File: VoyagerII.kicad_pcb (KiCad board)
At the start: 2 copper layers, 285 x 95.1 mm, 265 parts, among them P1 TC2030-IDC, SW1 SW_PUSH, U1 ATXMEGA32A4U-AU, U2 MCP1700T-3002E/TT, U3 PRTR5V0U2X, U4 IS31FL3731-SALS2, U5 74LVC1G34

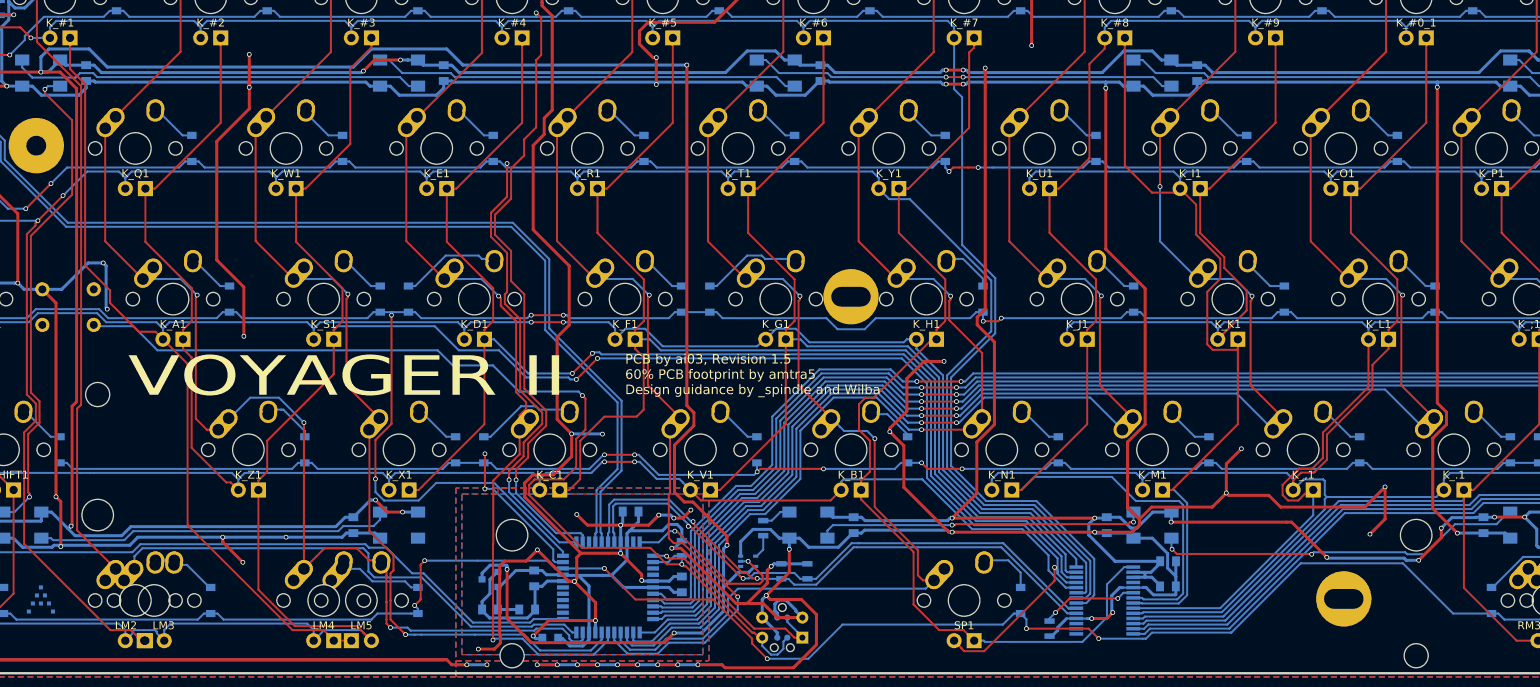
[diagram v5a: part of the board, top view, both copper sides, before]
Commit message: Tune up some traces
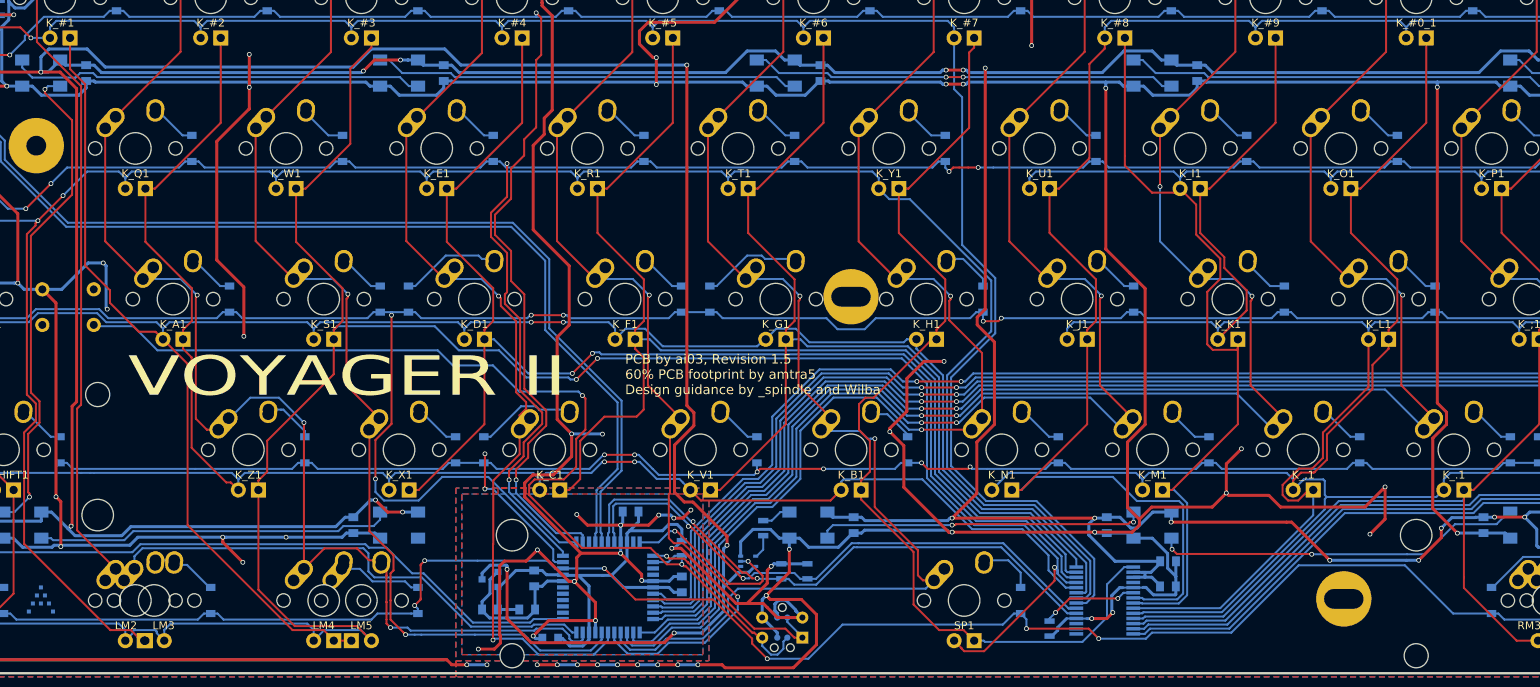
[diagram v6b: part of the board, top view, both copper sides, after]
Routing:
- net LED-B4: track 279.0 -> 278.2 mm
- net COL6: track 141.3 -> 142.0 mm
- net ROW2: track 334.0 -> 334.6 mm

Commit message: Unroute, prepare for LED chip replacement
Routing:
- net GND: track 1590.9 -> 0.00 mm, vias 74 -> 0
- net +5V: track 840.9 -> 0.00 mm, vias 22 -> 0
- net ROW0: track 340.1 -> 0.00 mm, vias 4 -> 0
- net LED-A1: track 336.7 -> 0.00 mm, vias 1 -> 0
- net ROW2: track 334.6 -> 0.00 mm, vias 6 -> 0
- net ROW1: track 327.0 -> 0.00 mm, vias 6 -> 0
- net COL14: track 316.5 -> 0.00 mm, vias 4 -> 0
- net LED-A5: track 301.0 -> 0.00 mm, vias 3 -> 0
- net LED-A2: track 294.3 -> 0.00 mm, vias 2 -> 0
- net LED-A3: track 279.0 -> 0.00 mm, vias 2 -> 0
- net LED-B4: track 278.2 -> 0.00 mm
- net ROW4: track 273.0 -> 0.00 mm, vias 6 -> 0
- net COL13: track 271.2 -> 0.00 mm, vias 4 -> 0
- net ROW3: track 267.4 -> 0.00 mm, vias 8 -> 0
- net COL12: track 258.2 -> 0.00 mm, vias 3 -> 0
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
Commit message: never mind
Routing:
- net GND: track 0.00 -> 1590.9 mm, vias 0 -> 74
- net +5V: track 0.00 -> 840.9 mm, vias 0 -> 22
- net ROW0: track 0.00 -> 340.1 mm, vias 0 -> 4
- net LED-A1: track 0.00 -> 336.7 mm, vias 0 -> 1
- net ROW2: track 0.00 -> 334.6 mm, vias 0 -> 6
- net ROW1: track 0.00 -> 327.0 mm, vias 0 -> 6
- net COL14: track 0.00 -> 316.5 mm, vias 0 -> 4
- net LED-A5: track 0.00 -> 301.0 mm, vias 0 -> 3
- net LED-A2: track 0.00 -> 294.3 mm, vias 0 -> 2
- net LED-A3: track 0.00 -> 279.0 mm, vias 0 -> 2
- net LED-B4: track 0.00 -> 278.2 mm
- net ROW4: track 0.00 -> 273.0 mm, vias 0 -> 6
- net COL13: track 0.00 -> 271.2 mm, vias 0 -> 4
- net ROW3: track 0.00 -> 267.4 mm, vias 0 -> 8
- net COL12: track 0.00 -> 258.2 mm, vias 0 -> 3
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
